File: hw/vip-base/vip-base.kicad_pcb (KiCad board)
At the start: 2 copper layers, 80 x 80 mm, 24 parts, among them J1 USB_C_Receptacle_USB2.0, J2 Conn_02x30_Odd_Even, J3 Conn_02x30_Odd_Even, U1 TLV62569DRL, U2 TLV62569DRL

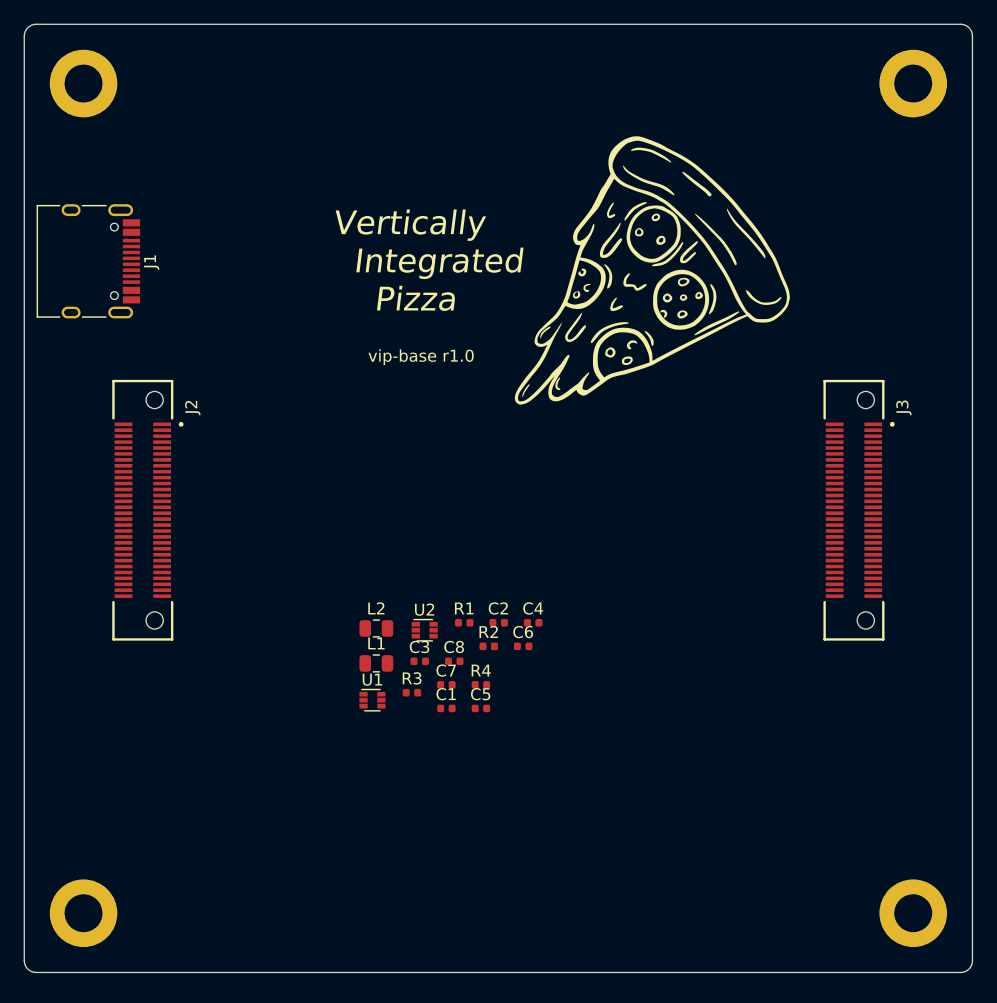
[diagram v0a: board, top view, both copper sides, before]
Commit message: hw: Finish main routing
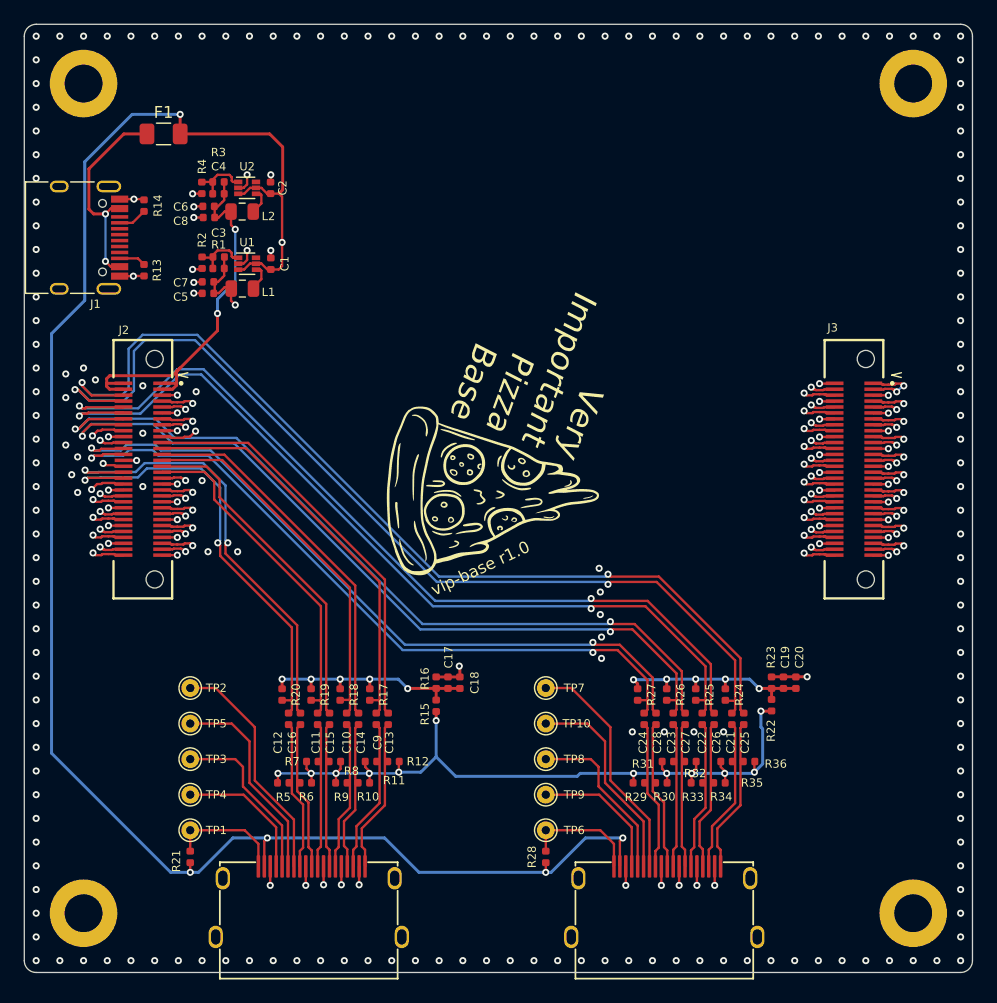
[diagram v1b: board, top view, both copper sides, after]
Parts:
- removed the G*** at (151.0, 88.0)
- added C10: 0.1u, Capacitor_SMD:C_0402_1005Metric, F.Cu at (127.2, 123.6)
- added C11: 0.1u, Capacitor_SMD:C_0402_1005Metric, F.Cu at (124.8, 123.6)
- added C12: 0.1u, Capacitor_SMD:C_0402_1005Metric, F.Cu at (122.3, 123.6)
- added C13: 0.1u, Capacitor_SMD:C_0402_1005Metric, F.Cu at (130.7, 123.6)
- added C14: 0.1u, Capacitor_SMD:C_0402_1005Metric, F.Cu at (128.2, 123.6)
- added C15: 0.1u, Capacitor_SMD:C_0402_1005Metric, F.Cu at (125.8, 123.6)
- added C16: 0.1u, Capacitor_SMD:C_0402_1005Metric, F.Cu at (123.3, 123.6)
- added C17: 0.1u, Capacitor_SMD:C_0402_1005Metric, F.Cu at (135.8, 120.5)
- added C18: 4.7u, Capacitor_SMD:C_0402_1005Metric, F.Cu at (136.8, 120.5)
- added C19: 0.1u, Capacitor_SMD:C_0402_1005Metric, F.Cu at (164.1, 120.5)
- added C20: 4.7u, Capacitor_SMD:C_0402_1005Metric, F.Cu at (165.1, 120.5)
- added C21: 0.1u, Capacitor_SMD:C_0402_1005Metric, F.Cu at (159.7, 123.6)
- added C22: 0.1u, Capacitor_SMD:C_0402_1005Metric, F.Cu at (157.2, 123.6)
- added C23: 0.1u, Capacitor_SMD:C_0402_1005Metric, F.Cu at (154.8, 123.6)
- added C24: 0.1u, Capacitor_SMD:C_0402_1005Metric, F.Cu at (152.3, 123.6)
- added C25: 0.1u, Capacitor_SMD:C_0402_1005Metric, F.Cu at (160.7, 123.6)
- added C26: 0.1u, Capacitor_SMD:C_0402_1005Metric, F.Cu at (158.2, 123.6)
- added C27: 0.1u, Capacitor_SMD:C_0402_1005Metric, F.Cu at (155.8, 123.6)
- added C28: 0.1u, Capacitor_SMD:C_0402_1005Metric, F.Cu at (153.3, 123.6)
- added C9: 0.1u, Capacitor_SMD:C_0402_1005Metric, F.Cu at (129.7, 123.6)
- added F1: Polyfuse_Small, Inductor_SMD:L_1206_3216Metric, F.Cu at (111.8, 74.2)
- added G***: LOGO, LOGO, F.Cu at (139.2, 104.5)
- added G***: LOGO, LOGO, B.Cu at (139.0, 104.5)
- added J4: HDMI_A_1.4, vip-base:HDMI-10029449-111RLF, F.Cu at (124.0, 137.0)
- added J5: HDMI_A_1.4, vip-base:HDMI-10029449-111RLF, F.Cu at (154.0, 137.0)
- added R10: 50R, Resistor_SMD:R_0402_1005Metric, F.Cu at (128.7, 129.0)
- added R11: 50R, Resistor_SMD:R_0402_1005Metric, F.Cu at (129.2, 127.2)
- added R12: 50R, Resistor_SMD:R_0402_1005Metric, F.Cu at (131.2, 127.2)
- added R13: 5.1k, Resistor_SMD:R_0402_1005Metric, F.Cu at (110.1, 85.8)
- added R14: 5.1k, Resistor_SMD:R_0402_1005Metric, F.Cu at (110.1, 80.3)
- added R15: 2k, Resistor_SMD:R_0402_1005Metric, F.Cu at (134.8, 122.5)
- added R16: 1k, Resistor_SMD:R_0402_1005Metric, F.Cu at (134.8, 120.5)
- added R17: 47k, Resistor_SMD:R_0402_1005Metric, F.Cu at (129.2, 121.5)
- added R18: 47k, Resistor_SMD:R_0402_1005Metric, F.Cu at (126.7, 121.5)
- added R19: 47k, Resistor_SMD:R_0402_1005Metric, F.Cu at (124.2, 121.5)
- added R20: 47k, Resistor_SMD:R_0402_1005Metric, F.Cu at (121.8, 121.5)
- added R21: 1k, Resistor_SMD:R_0402_1005Metric, F.Cu at (114.0, 135.2)
- added R22: 2k, Resistor_SMD:R_0402_1005Metric, F.Cu at (163.1, 122.5)
- added R23: 1k, Resistor_SMD:R_0402_1005Metric, F.Cu at (163.1, 120.5)
- added R24: 47k, Resistor_SMD:R_0402_1005Metric, F.Cu at (159.2, 121.5)
- added R25: 47k, Resistor_SMD:R_0402_1005Metric, F.Cu at (156.7, 121.5)
- added R26: 47k, Resistor_SMD:R_0402_1005Metric, F.Cu at (154.2, 121.5)
- added R27: 47k, Resistor_SMD:R_0402_1005Metric, F.Cu at (151.8, 121.5)
- added R28: 1k, Resistor_SMD:R_0402_1005Metric, F.Cu at (144.0, 135.2)
- added R29: 50R, Resistor_SMD:R_0402_1005Metric, F.Cu at (151.8, 129.0)
- added R30: 50R, Resistor_SMD:R_0402_1005Metric, F.Cu at (153.8, 129.0)
- added R31: 50R, Resistor_SMD:R_0402_1005Metric, F.Cu at (154.3, 127.2)
- added R32: 50R, Resistor_SMD:R_0402_1005Metric, F.Cu at (156.2, 127.2)
- added R33: 50R, Resistor_SMD:R_0402_1005Metric, F.Cu at (156.8, 129.0)
- added R34: 50R, Resistor_SMD:R_0402_1005Metric, F.Cu at (158.7, 129.0)
- added R35: 50R, Resistor_SMD:R_0402_1005Metric, F.Cu at (159.2, 127.2)
- added R36: 50R, Resistor_SMD:R_0402_1005Metric, F.Cu at (161.2, 127.2)
- added R5: 50R, Resistor_SMD:R_0402_1005Metric, F.Cu at (121.8, 129.0)
- added R6: 50R, Resistor_SMD:R_0402_1005Metric, F.Cu at (123.8, 129.0)
- added R7: 50R, Resistor_SMD:R_0402_1005Metric, F.Cu at (124.3, 127.2)
- added R8: 50R, Resistor_SMD:R_0402_1005Metric, F.Cu at (126.2, 127.2)
- added R9: 50R, Resistor_SMD:R_0402_1005Metric, F.Cu at (126.8, 129.0)
- added TP1: TestPoint, TestPoint:TestPoint_THTPad_D1.5mm_Drill0.7mm, F.Cu at (114.0, 133.0)
- added TP10: TestPoint, TestPoint:TestPoint_THTPad_D1.5mm_Drill0.7mm, F.Cu at (144.0, 124.0)
- added TP2: TestPoint, TestPoint:TestPoint_THTPad_D1.5mm_Drill0.7mm, F.Cu at (114.0, 121.0)
- added TP3: TestPoint, TestPoint:TestPoint_THTPad_D1.5mm_Drill0.7mm, F.Cu at (114.0, 127.0)
- added TP4: TestPoint, TestPoint:TestPoint_THTPad_D1.5mm_Drill0.7mm, F.Cu at (114.0, 130.0)
- added TP5: TestPoint, TestPoint:TestPoint_THTPad_D1.5mm_Drill0.7mm, F.Cu at (114.0, 124.0)
- added TP6: TestPoint, TestPoint:TestPoint_THTPad_D1.5mm_Drill0.7mm, F.Cu at (144.0, 133.0)
- added TP7: TestPoint, TestPoint:TestPoint_THTPad_D1.5mm_Drill0.7mm, F.Cu at (144.0, 121.0)
- added TP8: TestPoint, TestPoint:TestPoint_THTPad_D1.5mm_Drill0.7mm, F.Cu at (144.0, 127.0)
- added TP9: TestPoint, TestPoint:TestPoint_THTPad_D1.5mm_Drill0.7mm, F.Cu at (144.0, 130.0)
- moved R4 48.1 mm to (115.0, 78.8), turned to -90 degrees
- moved R3 46.1 mm to (116.4, 78.3)
- moved C6 45.6 mm to (115.5, 80.4)
- moved C4 44.9 mm to (116.4, 79.3)
- moved C8 42.8 mm to (115.6, 81.3)
- moved C5 41.9 mm to (115.5, 87.7)
- moved C2 41.4 mm to (120.8, 78.8), turned to -90 degrees
- moved R2 40.4 mm to (115.0, 85.1), turned to -90 degrees
- moved C1 40.3 mm to (120.8, 85.2), turned to -90 degrees
- moved U2 40.2 mm to (118.8, 78.8)
- moved C7 39.5 mm to (115.5, 86.7)
- moved U1 38.3 mm to (118.8, 85.2)
- moved C3 38.1 mm to (116.4, 84.6)
- moved L2 37.0 mm to (118.4, 80.8), turned to 180 degrees
- moved R1 36.4 mm to (116.4, 85.6)
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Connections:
- C1 pad 2: VSYS -> +5V
- C2 pad 2: VSYS -> +5V
- J1 pad A1: Net-(J1-PadA1) -> GND
- J1 pad A12: Net-(J1-PadA1) -> GND
- J1 pad A5: (no net) -> Net-(J1-PadA5)
- J1 pad A6: (no net) -> Net-(J1-PadA6)
- J1 pad A7: (no net) -> Net-(J1-PadA7)
- J1 pad A8: (no net) -> Net-(J1-PadA8)
- J1 pad B1: Net-(J1-PadA1) -> GND
- J1 pad B12: Net-(J1-PadA1) -> GND
- J1 pad B5: (no net) -> Net-(J1-PadB5)
- J1 pad B6: (no net) -> Net-(J1-PadB6)
- J1 pad B7: (no net) -> Net-(J1-PadB7)
- J1 pad B8: (no net) -> Net-(J1-PadB8)
- J1 pad S1: Net-(J1-PadS1) -> GND
- J2 pad 10: (no net) -> /HDMI1.D1_P
- J2 pad 11: (no net) -> Net-(J2-Pad11)
- J2 pad 12: (no net) -> /HDMI1.D1_N
- J2 pad 13: (no net) -> Net-(J2-Pad13)
- J2 pad 14: (no net) -> /HDMI1.D0_P
- J2 pad 15: (no net) -> Net-(J2-Pad15)
- J2 pad 16: (no net) -> /HDMI1.D0_N
- J2 pad 17: /upstream_connectors/GND -> GND
- J2 pad 18: /upstream_connectors/GND -> GND
- J2 pad 19: /upstream_connectors/GND -> GND
- J2 pad 20: /upstream_connectors/GND -> GND
- J2 pad 21: (no net) -> /HDMI0.D2_P
- J2 pad 22: /upstream_connectors/GND -> GND
- J2 pad 23: (no net) -> /HDMI0.D2_N
- J2 pad 24: (no net) -> /HDMI1.CK_P
- J2 pad 25: (no net) -> /HDMI0.D1_P
- J2 pad 26: (no net) -> /HDMI1.CK_N
- J2 pad 27: (no net) -> /HDMI0.D1_N
- J2 pad 28: (no net) -> Net-(J2-Pad28)
- J2 pad 29: (no net) -> /HDMI0.D0_P
- J2 pad 30: (no net) -> Net-(J2-Pad30)
- J2 pad 31: (no net) -> /HDMI0.D0_N
- J2 pad 32: (no net) -> /HDMI0.CK_P
- J2 pad 33: /upstream_connectors/GND -> GND
- J2 pad 34: (no net) -> /HDMI0.CK_N
- J2 pad 35: /upstream_connectors/GND -> GND
- J2 pad 36: /upstream_connectors/GND -> GND
- J2 pad 37: (no net) -> Net-(J2-Pad37)
- J2 pad 38: /upstream_connectors/GND -> GND
- J2 pad 39: (no net) -> Net-(J2-Pad39)
- J2 pad 40: /upstream_connectors/GND -> GND
- J2 pad 41: (no net) -> Net-(J2-Pad41)
- J2 pad 42: (no net) -> Net-(J2-Pad42)
- J2 pad 43: (no net) -> Net-(J2-Pad43)
- J2 pad 44: (no net) -> Net-(J2-Pad44)
- J2 pad 45: (no net) -> Net-(J2-Pad45)
- J2 pad 46: (no net) -> Net-(J2-Pad46)
- J2 pad 47: (no net) -> Net-(J2-Pad47)
- J2 pad 48: (no net) -> Net-(J2-Pad48)
- J2 pad 49: (no net) -> Net-(J2-Pad49)
- J2 pad 50: (no net) -> Net-(J2-Pad50)
- J2 pad 51: (no net) -> Net-(J2-Pad51)
- J2 pad 52: (no net) -> Net-(J2-Pad52)
- J2 pad 53: /upstream_connectors/GND -> GND
- J2 pad 54: /upstream_connectors/GND -> GND
- J2 pad 55: /upstream_connectors/GND -> GND
- J2 pad 56: /upstream_connectors/GND -> GND
- J3 pad 10: (no net) -> Net-(J3-Pad10)
- J3 pad 11: /upstream_connectors/GND -> GND
- J3 pad 12: (no net) -> Net-(J3-Pad12)
- J3 pad 13: (no net) -> Net-(J3-Pad13)
- J3 pad 14: /upstream_connectors/GND -> GND
- J3 pad 15: (no net) -> Net-(J3-Pad15)
- J3 pad 16: (no net) -> Net-(J3-Pad16)
- J3 pad 17: /upstream_connectors/GND -> GND
- J3 pad 18: (no net) -> Net-(J3-Pad18)
- J3 pad 19: (no net) -> Net-(J3-Pad19)
- J3 pad 20: /upstream_connectors/GND -> GND
- J3 pad 21: (no net) -> Net-(J3-Pad21)
- J3 pad 23: (no net) -> Net-(J3-Pad23)
- J3 pad 25: (no net) -> Net-(J3-Pad25)
- J3 pad 26: /upstream_connectors/GND -> GND
- J3 pad 27: (no net) -> Net-(J3-Pad27)
- J3 pad 28: (no net) -> /upstream_connectors/GSRN
- J3 pad 29: (no net) -> Net-(J3-Pad29)
- J3 pad 30: (no net) -> Net-(J3-Pad30)
- J3 pad 31: (no net) -> Net-(J3-Pad31)
- J3 pad 32: (no net) -> Net-(J3-Pad32)
- J3 pad 33: (no net) -> Net-(J3-Pad33)
- J3 pad 34: /upstream_connectors/GND -> GND
- J3 pad 35: (no net) -> Net-(J3-Pad35)
- J3 pad 36: (no net) -> Net-(J3-Pad36)
- J3 pad 37: (no net) -> Net-(J3-Pad37)
- J3 pad 38: (no net) -> Net-(J3-Pad38)
- J3 pad 39: (no net) -> Net-(J3-Pad39)
- J3 pad 40: /upstream_connectors/GND -> GND
- J3 pad 41: (no net) -> Net-(J3-Pad41)
- J3 pad 42: (no net) -> Net-(J3-Pad42)
- J3 pad 43: (no net) -> Net-(J3-Pad43)
- J3 pad 44: (no net) -> Net-(J3-Pad44)
- J3 pad 45: (no net) -> Net-(J3-Pad45)
- J3 pad 46: /upstream_connectors/GND -> GND
- J3 pad 47: (no net) -> Net-(J3-Pad47)
- J3 pad 48: (no net) -> Net-(J3-Pad48)
- J3 pad 49: (no net) -> Net-(J3-Pad49)
- J3 pad 50: (no net) -> Net-(J3-Pad50)
- J3 pad 51: (no net) -> Net-(J3-Pad51)
- J3 pad 52: /upstream_connectors/GND -> GND
- J3 pad 53: (no net) -> Net-(J3-Pad53)
- J3 pad 54: (no net) -> Net-(J3-Pad54)
- J3 pad 55: /upstream_connectors/GND -> GND
- J3 pad 56: (no net) -> Net-(J3-Pad56)
- J3 pad 57: /upstream_connectors/GND -> GND
- J3 pad 58: /upstream_connectors/GND -> GND
- J3 pad 59: /upstream_connectors/GND -> GND
- J3 pad 60: (no net) -> Net-(J3-Pad60)
- U1 pad 3: VSYS -> +5V
- U1 pad 5: VSYS -> +5V
- U1 pad 6: (no net) -> Net-(U1-Pad6)
- U2 pad 3: VSYS -> +5V
- U2 pad 5: VSYS -> +5V
- U2 pad 6: (no net) -> Net-(U2-Pad6)
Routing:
- net +5V: track 0.00 -> 209.5 mm, vias 0 -> 9
- net P2.5V: track 0.00 -> 116.8 mm, vias 0 -> 7
- net P3.3V: track 0.00 -> 102.5 mm, vias 0 -> 4
- net GND: track 0.00 -> 89.0 mm, vias 0 -> 233
- net /HDMI1.D2_N: track 0.00 -> 81.4 mm, vias 0 -> 2
- net /HDMI1.D2_P: track 0.00 -> 80.5 mm, vias 0 -> 2
- net /HDMI1.D1_N: track 0.00 -> 73.4 mm, vias 0 -> 2
- net /HDMI1.D1_P: track 0.00 -> 73.3 mm, vias 0 -> 2
- net /HDMI1.D0_P: track 0.00 -> 68.6 mm, vias 0 -> 2
- net /HDMI1.D0_N: track 0.00 -> 67.9 mm, vias 0 -> 2
- net +3V3: track 0.00 -> 67.1 mm, vias 0 -> 12
- net /HDMI1.CK_N: track 0.00 -> 62.0 mm, vias 0 -> 2
- net /HDMI1.CK_P: track 0.00 -> 61.9 mm, vias 0 -> 2
- net /HDMI0.CK_N: track 0.00 -> 38.5 mm, vias 0 -> 2
- net /HDMI0.CK_P: track 0.00 -> 38.4 mm, vias 0 -> 2
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- added copper zone on In1.Cu, net GND
- added copper zone on In2.Cu, net GND
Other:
- copper layers 2 -> 4
- board text added: "Very Important Pizza Base"
- board text removed: "Vertically Integrated Pizza"

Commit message: hw: Add gerbers
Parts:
- added G***: LOGO, gsd_logo_small, F.Cu at (103.0, 77.0)
- added G***: LOGO, oshw_small, F.Cu at (105.0, 91.0)
- moved G*** 1.27 mm to (138.3, 103.6), turned to 0 degrees
- moved G*** 1.09 mm to (138.6, 103.5), turned to 180 degrees
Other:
- board text added: "https://github.com/gregdavill/vip-base"
